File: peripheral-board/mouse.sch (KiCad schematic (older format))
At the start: 1 part, among them U3001 PSPNUB

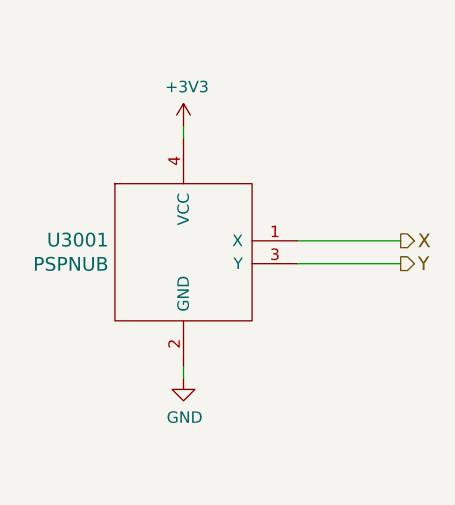
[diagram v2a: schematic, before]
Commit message: mouse connected to adc pins
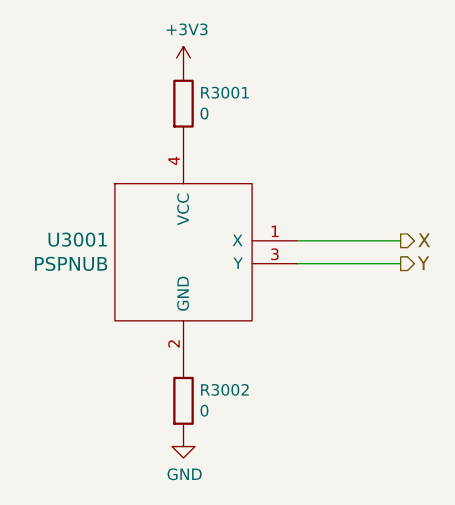
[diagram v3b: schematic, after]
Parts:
- added R3001, R3002: 0, Resistors_SMD:R_1206, symbol R
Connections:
- net +3V3: now also R3001.1; no longer U3001.4 (VCC)
- net GND: now also R3002.2; no longer U3001.2 (GND)
- new net: R3002.1, U3001.2 (GND)
- new net: R3001.2, U3001.4 (VCC)
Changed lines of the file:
@@
 L +3V3 #PWR034
 U 1 1 582269F3
-P 5100 2050
-F 0 "#PWR034" H 5100 1900 50  0001 C CNN
-F 1 "+3V3" H 5115 2223 50  0000 C CNN
-F 2 "" H 5100 2050 50  0000 C CNN
-F 3 "" H 5100 2050 50  0000 C CNN
-	1    5100 2050
+P 5100 1800
+F 0 "#PWR034" H 5100 1650 50  0001 C CNN
+F 1 "+3V3" H 5115 1973 50  0000 C CNN
+F 2 "" H 5100 1800 50  0000 C CNN
+F 3 "" H 5100 1800 50  0000 C CNN
+	1    5100 1800
 	1    0    0    -1
 $EndComp
@@
 L GND #PWR035
 U 1 1 58226A0A
-P 5100 3150
-F 0 "#PWR035" H 5100 2900 50  0001 C CNN
-F 1 "GND" H 5105 2977 50  0000 C CNN
-F 2 "" H 5100 3150 50  0000 C CNN
-F 3 "" H 5100 3150 50  0000 C CNN
-	1    5100 3150
+P 5100 3400
+F 0 "#PWR035" H 5100 3150 50  0001 C CNN
+F 1 "GND" H 5105 3227 50  0000 C CNN
+F 2 "" H 5100 3400 50  0000 C CNN
+F 3 "" H 5100 3400 50  0000 C CNN
+	1    5100 3400
 	1    0    0    -1
 $EndComp
-Wire Wire Line
-	5100 2050 5100 2100
-Wire Wire Line
-	5100 3100 5100 3150
 Text HLabel 6050 2550 2    60   Output ~ 0
 X
@@
 Wire Wire Line
 	5600 2650 6050 2650
+$Comp
+L R R3001
+U 1 1 58E56E4E
+P 5100 1950
+F 0 "R3001" H 5170 1996 50  0000 L CNN
+F 1 "0" H 5170 1905 50  0000 L CNN
+F 2 "Resistors_SMD:R_1206" V 5030 1950 50  0001 C CNN
+F 3 "" H 5100 1950 50  0001 C CNN
+	1    5100 1950
+	1    0    0    -1
+$EndComp
+$Comp
+L R R3002
+U 1 1 58E56F28
+P 5100 3250
+F 0 "R3002" H 5170 3296 50  0000 L CNN
+F 1 "0" H 5170 3205 50  0000 L CNN
+F 2 "Resistors_SMD:R_1206" V 5030 3250 50  0001 C CNN
+F 3 "" H 5100 3250 50  0001 C CNN
+	1    5100 3250
+	1    0    0    -1
+$EndComp
 $EndSCHEMATC
